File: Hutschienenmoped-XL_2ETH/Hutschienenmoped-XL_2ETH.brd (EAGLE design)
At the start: 166.3 x 101.8 mm, 129 parts, among them J1 638207222005, J13 638207222005, J15 638207222008, J2 645004114822, J4 61300421121, J7 638207222005, J8 638207222007, U4 TLE9250VSJ

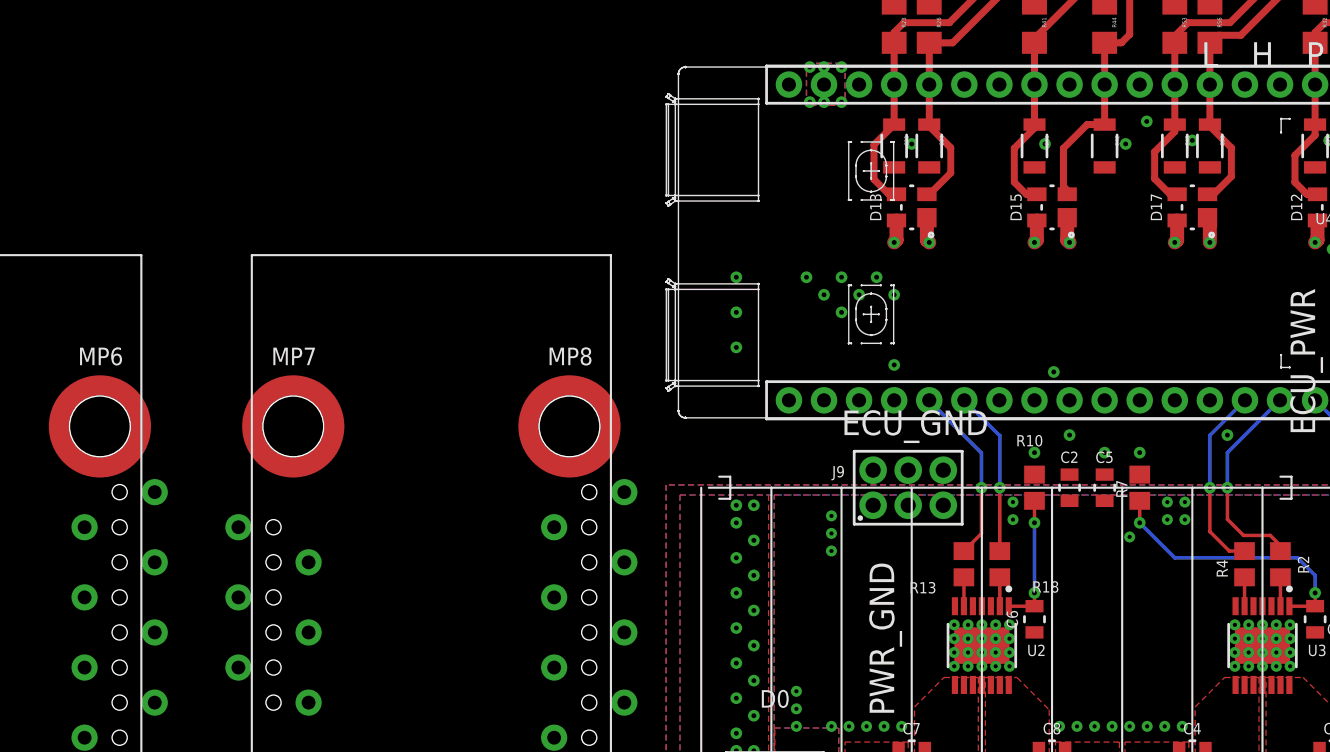
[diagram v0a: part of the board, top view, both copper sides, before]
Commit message: Update grid settings, layer visibility, and parameters. Refine wire connections for improved layout consistency.
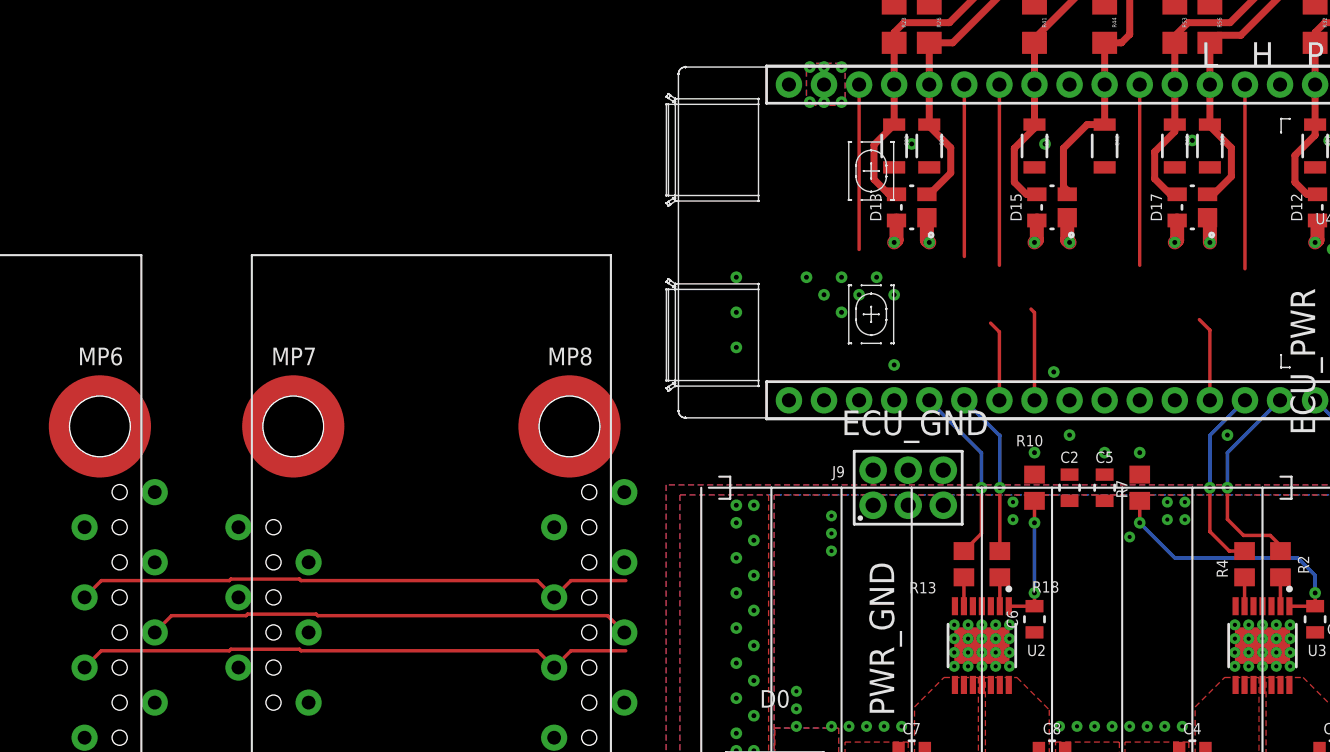
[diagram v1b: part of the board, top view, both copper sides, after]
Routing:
- net SCLK: track 0.00 -> 53.9 mm
- net MOSI: track 0.00 -> 53.2 mm
- net MISO: track 0.00 -> 47.0 mm
- net RST0: track 0.00 -> 13.3 mm
- net CS1: track 0.00 -> 13.1 mm
- net INT1: track 0.00 -> 6.71 mm
- net RST1: track 0.00 -> 6.16 mm
- net INT0: track 0.00 -> 5.85 mm
- net ECU_GND: vias 92 -> 90
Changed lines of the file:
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@@
 <setting verticaltext="up"/>
 </settings>
-<grid distance="1" unitdist="mm" unit="mm" style="lines" multiple="1" display="yes" altdistance="5" altunitdist="mil" altunit="mil"/>
+<grid distance="5" unitdist="mil" unit="mil" style="lines" multiple="1" display="yes" altdistance="5" altunitdist="mil" altunit="mil"/>
 <layers>
 <layer number="1" name="Top" color="4" fill="1" visible="yes" active="yes"/>
@@
 <layer number="15" name="Route15" color="23" fill="1" visible="no" active="yes"/>
 <layer number="16" name="Bottom" color="1" fill="1" visible="yes" active="yes"/>
-<layer number="17" name="Pads" color="2" fill="1" visible="no" active="yes"/>
+<layer number="17" name="Pads" color="2" fill="1" visible="yes" active="yes"/>
 <layer number="18" name="Vias" color="2" fill="1" visible="yes" active="yes"/>
-<layer number="19" name="Unrouted" color="6" fill="1" visible="no" active="yes"/>
+<layer number="19" name="Unrouted" color="6" fill="1" visible="yes" active="yes"/>
 <layer number="20" name="Dimension" color="24" fill="1" visible="no" active="yes"/>
 <layer number="21" name="tPlace" color="7" fill="1" visible="no" active="yes"/>
@@
 <layer number="42" name="bRestrict" color="1" fill="10" visible="no" active="yes"/>
 <layer number="43" name="vRestrict" color="2" fill="10" visible="no" active="yes"/>
-<layer number="44" name="Drills" color="7" fill="1" visible="no" active="yes"/>
-<layer number="45" name="Holes" color="7" fill="1" visible="no" active="yes"/>
+<layer number="44" name="Drills" color="7" fill="1" visible="yes" active="yes"/>
+<layer number="45" name="Holes" color="7" fill="1" visible="yes" active="yes"/>
 <layer number="46" name="Milling" color="3" fill="1" visible="no" active="yes"/>
 <layer number="47" name="Measures" color="7" fill="1" visible="no" active="yes"/>
@@
 <param name="mdViaViaSameLayer" value="0.2mm"/>
 <param name="mnLayersViaInSmd" value="2"/>
-<param name="mdCopperDimension" value="0.2mm"/>
-<param name="mdDrill" value="0.2mm"/>
+<param name="mdCopperDimension" value="0.5mm"/>
+<param name="mdDrill" value="0.5mm"/>
 <param name="mdSmdStop" value="0mil"/>
 <param name="msWidth" value="0.25mm"/>
@@
 <wire x1="53.975" y1="64.475" x2="53.975" y2="61.84" width="1.016" layer="1"/>
 <via x="38.1" y="65.806" extent="1-16" drill="0.35"/>
-<via x="34.798" y="67.183" extent="1-16" drill="0.35"/>
-<via x="33.274" y="65.552" extent="1-16" drill="0.35"/>
 <via x="27.432" y="65.552" extent="1-16" drill="0.35"/>
 <via x="17.78" y="65.552" extent="1-16" drill="0.35"/>
@@
 <contactref element="W2-J1" pad="3"/>
 <contactref element="ESP32-J1" pad="17"/>
-<wire x1="-8.11" y1="27.64" x2="21.59" y2="69.85" width="0" layer="19" extent="1-1"/>
-<wire x1="-42.11" y1="27.64" x2="-8.11" y2="27.64" width="0" layer="19" extent="1-1"/>
+<wire x1="-42.11" y1="27.64" x2="-40.895" y2="28.855" width="0.25" layer="1"/>
+<wire x1="-8.11" y1="27.64" x2="-9.325" y2="28.855" width="0.25" layer="1"/>
+<wire x1="-26.4388375" y1="28.855" x2="-9.325" y2="28.855" width="0.25" layer="1"/>
+<wire x1="-31.6288375" y1="28.855" x2="-31.5188375" y2="28.965" width="0.25" layer="1"/>
+<wire x1="-26.5488375" y1="28.965" x2="-26.4388375" y2="28.855" width="0.25" layer="1"/>
+<wire x1="-40.895" y1="28.855" x2="-31.6288375" y2="28.855" width="0.25" layer="1"/>
+<wire x1="-31.5188375" y1="28.965" x2="-26.5488375" y2="28.965" width="0.25" layer="1"/>
+<wire x1="-8.11" y1="27.64" x2="-6.895" y2="28.855" width="0.25" layer="1"/>
+<wire x1="-6.895" y1="28.855" x2="-2.921" y2="28.855" width="0.25" layer="1"/>
+<wire x1="21.59" y1="69.85" x2="21.59" y2="57.404" width="0.25" layer="1"/>
+<wire x1="-2.921" y1="28.855" x2="21.59" y2="57.404" width="0" layer="19" extent="1-1"/>
 </signal>
 <signal name="MISO">
@@
 <contactref element="W1-J1" pad="4"/>
 <contactref element="ESP32-J1" pad="20"/>
-<wire x1="-3.03" y1="30.18" x2="13.97" y2="69.85" width="0" layer="19" extent="1-1"/>
-<wire x1="-37.03" y1="30.18" x2="-3.03" y2="30.18" width="0" layer="19" extent="1-1"/>
+<wire x1="-37.03" y1="30.18" x2="-35.815" y2="31.395" width="0.25" layer="1"/>
+<wire x1="-30.4211625" y1="31.395" x2="-35.815" y2="31.395" width="0.25" layer="1"/>
+<wire x1="-3.03" y1="30.18" x2="-4.245" y2="31.395" width="0.25" layer="1"/>
+<wire x1="-25.2311625" y1="31.395" x2="-25.3411625" y2="31.505" width="0.25" layer="1"/>
+<wire x1="-30.3111625" y1="31.505" x2="-30.4211625" y2="31.395" width="0.25" layer="1"/>
+<wire x1="-4.245" y1="31.395" x2="-25.2311625" y2="31.395" width="0.25" layer="1"/>
+<wire x1="-25.3411625" y1="31.505" x2="-30.3111625" y2="31.505" width="0.25" layer="1"/>
+<wire x1="13.97" y1="69.85" x2="13.97" y2="57.912" width="0.25" layer="1"/>
+<wire x1="-3.03" y1="30.18" x2="13.97" y2="57.912" width="0" layer="19" extent="1-1"/>
 </signal>
 <signal name="SCLK">
@@
 <contactref element="W2-J1" pad="5"/>
 <contactref element="ESP32-J1" pad="16"/>
-<wire x1="-8.11" y1="32.72" x2="24.13" y2="69.85" width="0" layer="19" extent="1-1"/>
-<wire x1="-42.11" y1="32.72" x2="-8.11" y2="32.72" width="0" layer="19" extent="1-1"/>
+<wire x1="-42.11" y1="32.72" x2="-40.895" y2="33.935" width="0.25" layer="1"/>
+<wire x1="-8.11" y1="32.72" x2="-9.325" y2="33.935" width="0.25" layer="1"/>
+<wire x1="-26.4388375" y1="33.935" x2="-9.325" y2="33.935" width="0.25" layer="1"/>
+<wire x1="-31.6288375" y1="33.935" x2="-31.5188375" y2="34.045" width="0.25" layer="1"/>
+<wire x1="-26.5488375" y1="34.045" x2="-26.4388375" y2="33.935" width="0.25" layer="1"/>
+<wire x1="-40.895" y1="33.935" x2="-31.6288375" y2="33.935" width="0.25" layer="1"/>
+<wire x1="-31.5188375" y1="34.045" x2="-26.5488375" y2="34.045" width="0.25" layer="1"/>
+<wire x1="-8.11" y1="32.72" x2="-6.895" y2="33.935" width="0.25" layer="1"/>
+<wire x1="-6.895" y1="33.935" x2="-2.921" y2="33.935" width="0.25" layer="1"/>
+<wire x1="24.13" y1="69.85" x2="24.13" y2="56.769" width="0.25" layer="1"/>
+<wire x1="-2.921" y1="33.935" x2="24.13" y2="56.769" width="0" layer="19" extent="1-1"/>
 </signal>
 <signal name="CS0">
@@
 <contactref element="W2-J1" pad="6"/>
 <contactref element="ESP32-J1" pad="12"/>
-<wire x1="-3.03" y1="35.26" x2="34.29" y2="69.85" width="0" layer="19" extent="1-1"/>
+<wire x1="34.29" y1="69.85" x2="34.29" y2="56.769" width="0.25" layer="1"/>
+<wire x1="-3.03" y1="35.26" x2="34.29" y2="56.769" width="0" layer="19" extent="1-1"/>
 </signal>
 <signal name="INT0">
 <contactref element="W1-J2" pad="5"/>
 <contactref element="ESP32-J3" pad="16"/>
+<wire x1="24.13" y1="46.99" x2="24.13" y2="51.943" width="0.25" layer="1"/>
+<wire x1="24.13" y1="51.943" x2="23.495" y2="52.578" width="0.25" layer="1"/>
 <wire x1="-59.89" y1="35.26" x2="24.13" y2="46.99" width="0" layer="19" extent="1-1"/>
 </signal>
@@
 <contactref element="W2-J2" pad="5"/>
 <contactref element="ESP32-J3" pad="15"/>
+<wire x1="26.67" y1="46.99" x2="26.67" y2="53.34" width="0.25" layer="1"/>
+<wire x1="26.67" y1="53.34" x2="26.416" y2="53.594" width="0.25" layer="1"/>
 <wire x1="-25.89" y1="35.26" x2="26.67" y2="46.99" width="0" layer="19" extent="1-1"/>
 </signal>
@@
 <contactref element="W2-J2" pad="3"/>
 <contactref element="ESP32-J3" pad="10"/>
+<wire x1="39.37" y1="46.99" x2="39.37" y2="52.07" width="0.25" layer="1"/>
+<wire x1="39.37" y1="52.07" x2="38.608" y2="52.832" width="0.25" layer="1"/>
 <wire x1="-25.89" y1="30.18" x2="39.37" y2="46.99" width="0" layer="19" extent="1-1"/>
 </signal>
@@
 <contactref element="W1-J2" pad="3"/>
 <contactref element="ESP32-J1" pad="9"/>
-<wire x1="-59.89" y1="30.18" x2="41.91" y2="69.85" width="0" layer="19" extent="1-1"/>
+<wire x1="41.91" y1="69.85" x2="41.91" y2="56.515" width="0.25" layer="1"/>
+<wire x1="-59.89" y1="30.18" x2="41.91" y2="56.515" width="0" layer="19" extent="1-1"/>
 </signal>
 </signals>

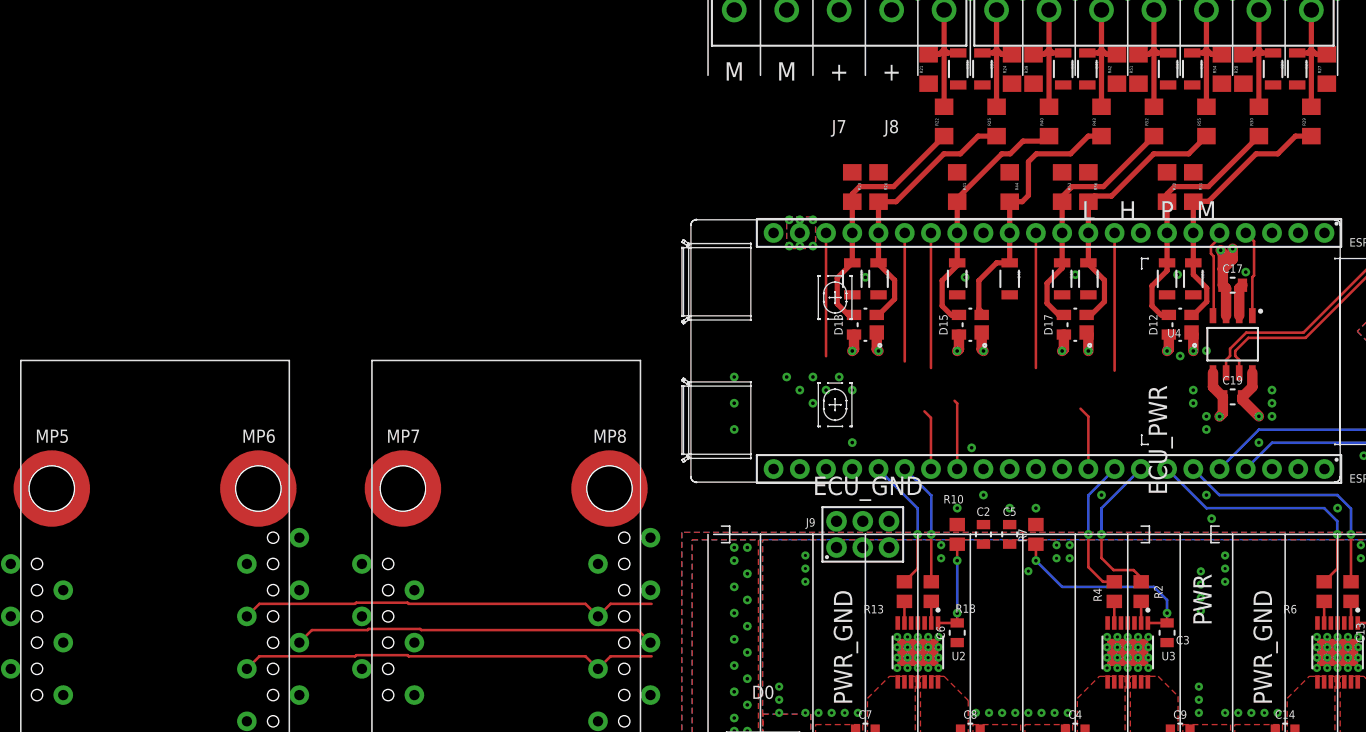
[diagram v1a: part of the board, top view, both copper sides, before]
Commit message: Change grid unit from mil to mm, adjust polygon width, add contact references for elements J13 and J9, update via drill sizes, modify wire connections for various signals.
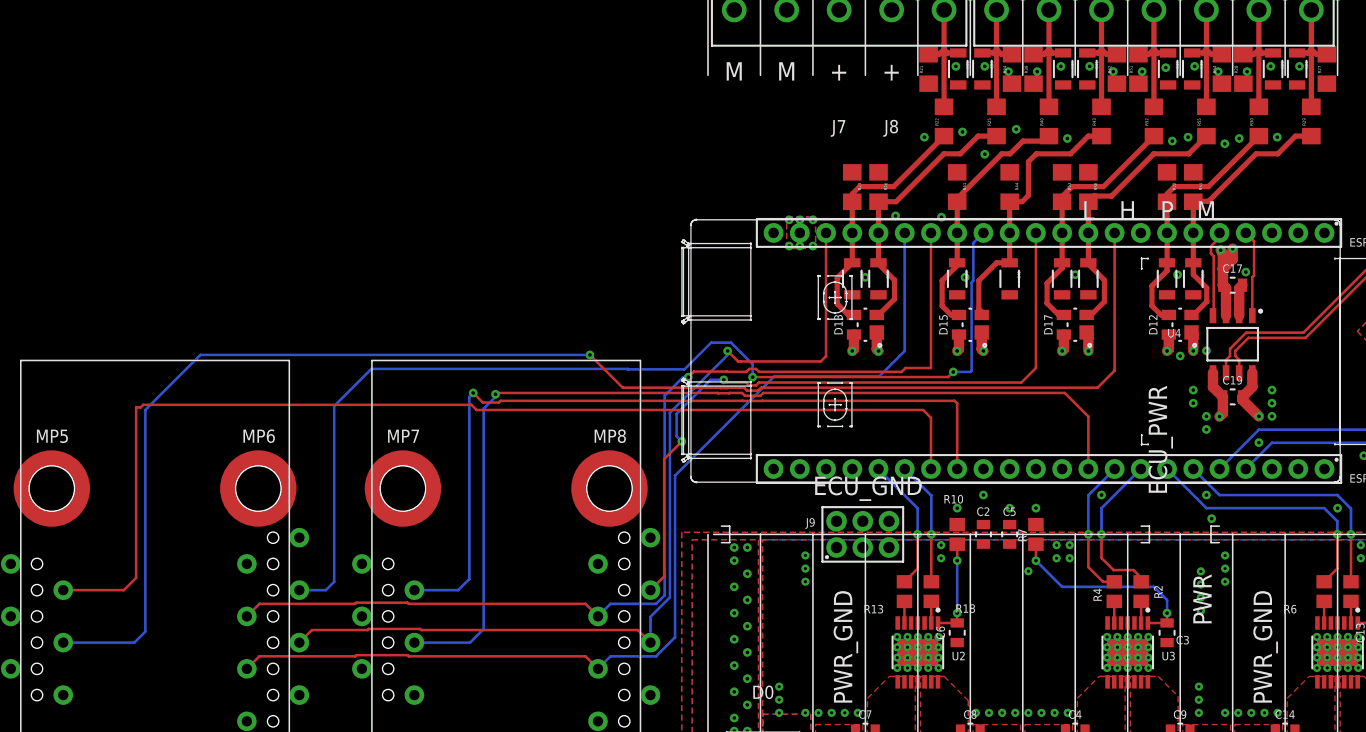
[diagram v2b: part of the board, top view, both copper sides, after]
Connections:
- removed net N$20: J13.5, J13.A5
- net PWR_GND: now also J13.5, J13.A5
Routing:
- net RST0: track 13.3 -> 141.5 mm, vias 0 -> 1
- net CS0: track 0.00 -> 101.2 mm, vias 0 -> 2
- net INT0: track 5.85 -> 106.6 mm
- net RST1: track 6.16 -> 94.2 mm, vias 0 -> 1
- net INT1: track 6.71 -> 77.7 mm, vias 0 -> 1
- net CS1: track 13.1 -> 68.7 mm, vias 0 -> 2
- net SCLK: track 53.9 -> 102.0 mm, vias 0 -> 1
- net MOSI: track 53.2 -> 98.2 mm
- net MISO: track 47.0 -> 88.5 mm, vias 0 -> 1
- net ECU_GND: vias 90 -> 104
